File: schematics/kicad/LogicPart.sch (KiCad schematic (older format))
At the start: 19 parts, among them P2 USB_OTG, P3 CONN_02X03, U6 SST25VF020B, U7 ATMEGA32U4-A, Y1 Crystal

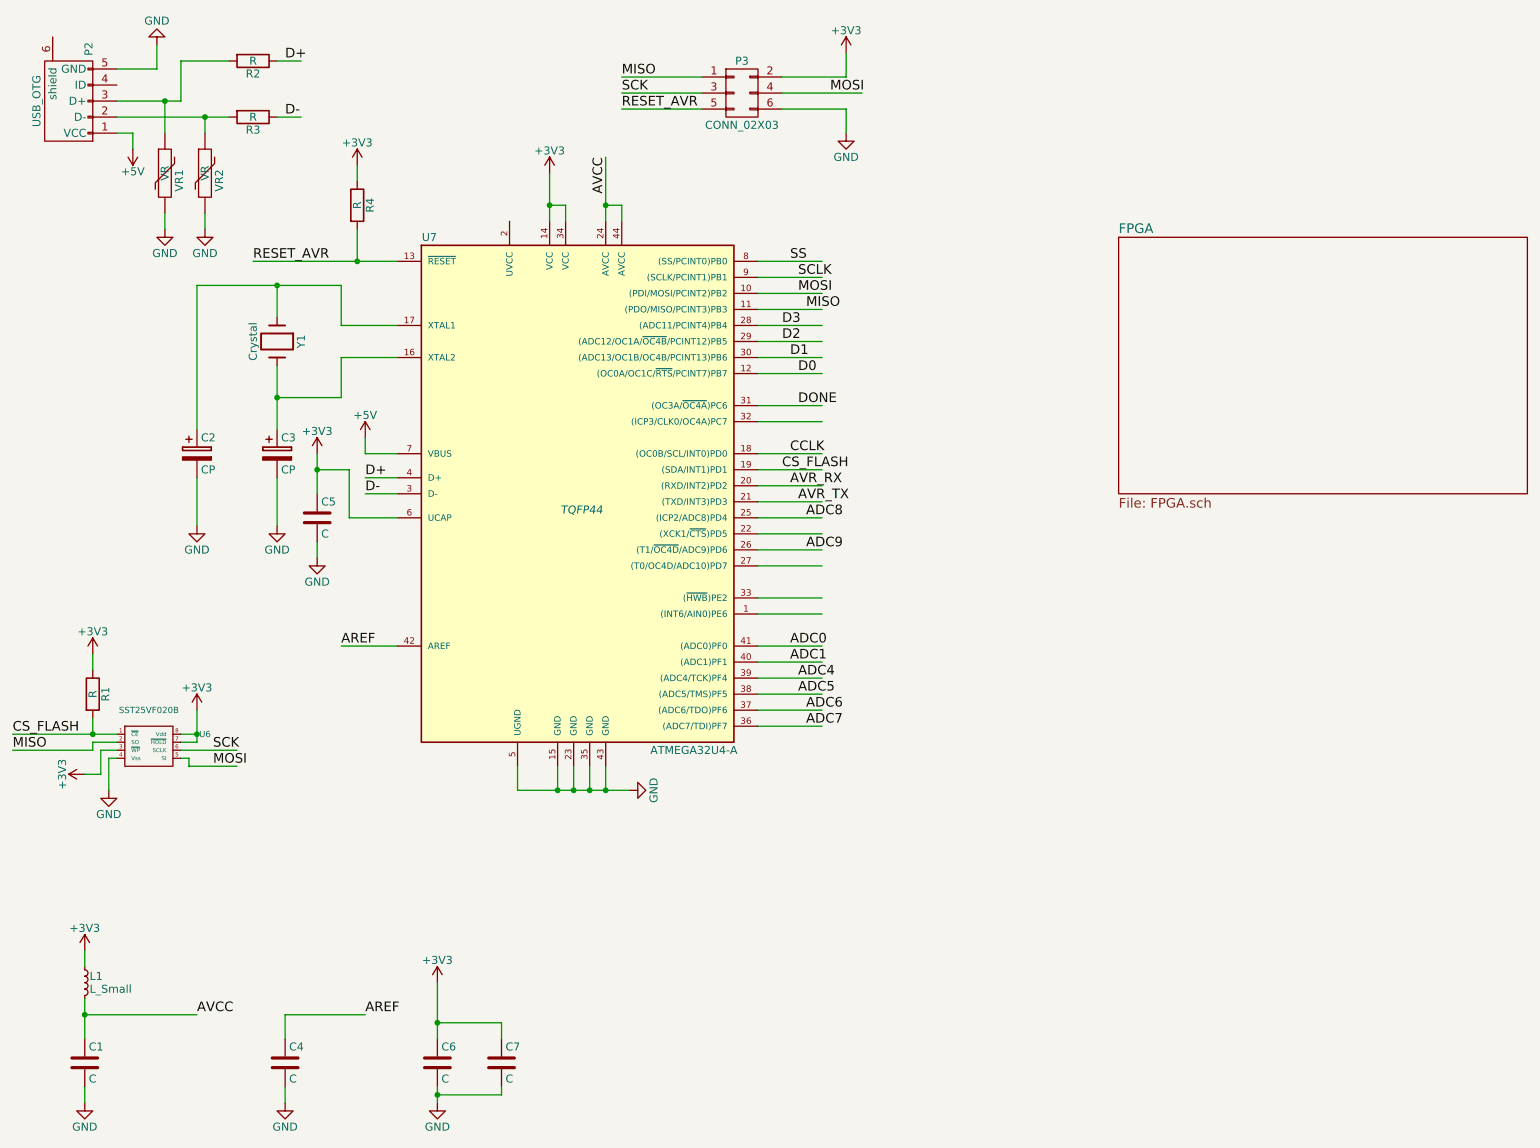
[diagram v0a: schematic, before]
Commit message: Change a lot of things, especially pinning between sheets
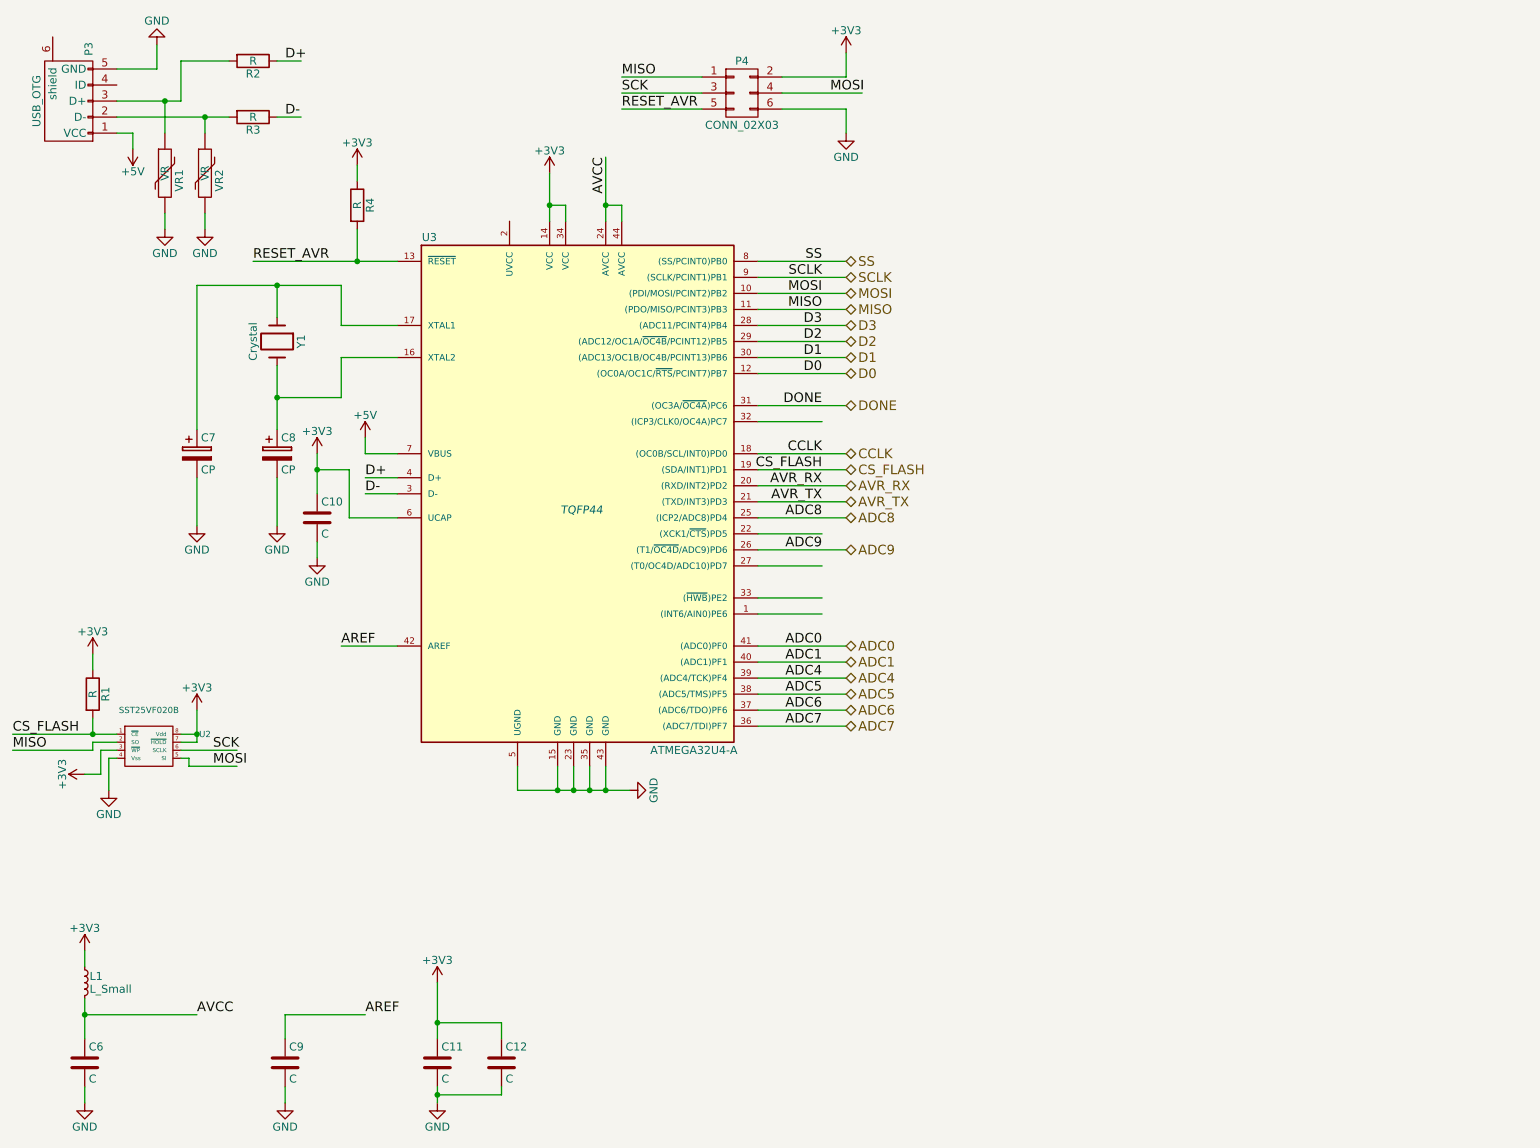
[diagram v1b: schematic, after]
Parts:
- renumbered C5 to C10, C6 to C11, C7 to C12, C1 to C6, C2 to C7, C3 to C8, C4 to C9, P2 to P3, P3 to P4, U6 to U2, U7 to U3
